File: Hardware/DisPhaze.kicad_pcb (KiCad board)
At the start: 2 copper layers, 60 x 110 mm, 76 parts, among them J1 SWD_Header, J2 PItch_In, J3 PD1_Amt_In, J4 PD2_Amt_In, J5 VCA_In, J6 DAC1_Out, J7 DAC2_Out, J8 Eurorack_16_pin_power, SW1 DAC1_RingMod_Switch, SW2 DAC2_Mix_Switch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

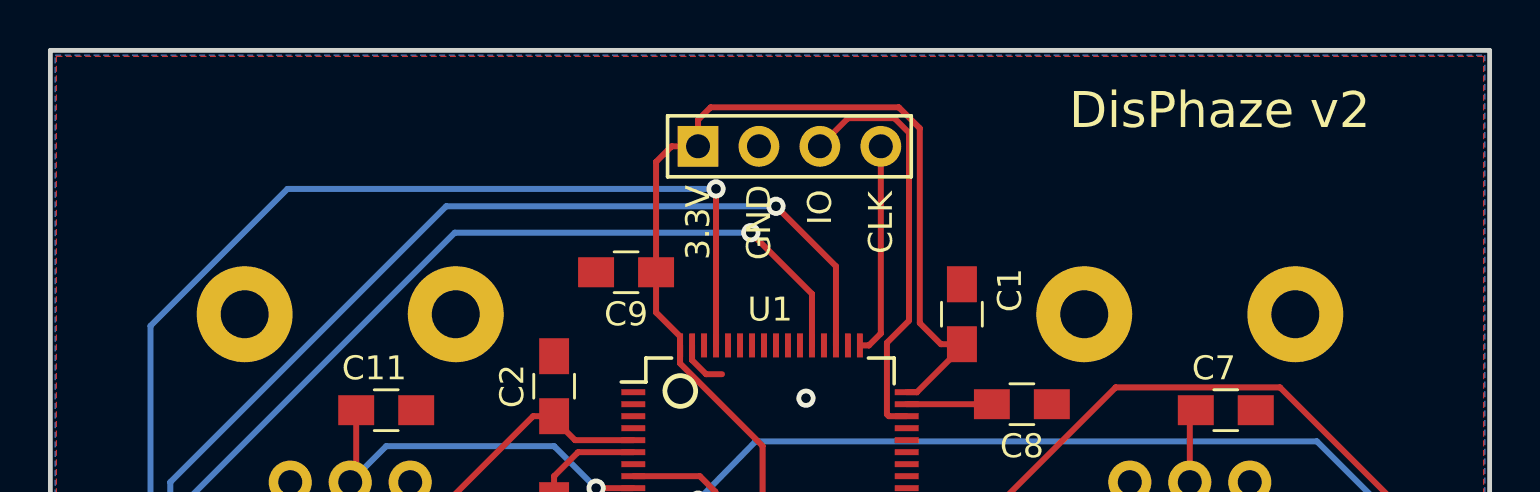
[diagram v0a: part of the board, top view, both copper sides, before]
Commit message: Added basic calibration and further tweaks to panel
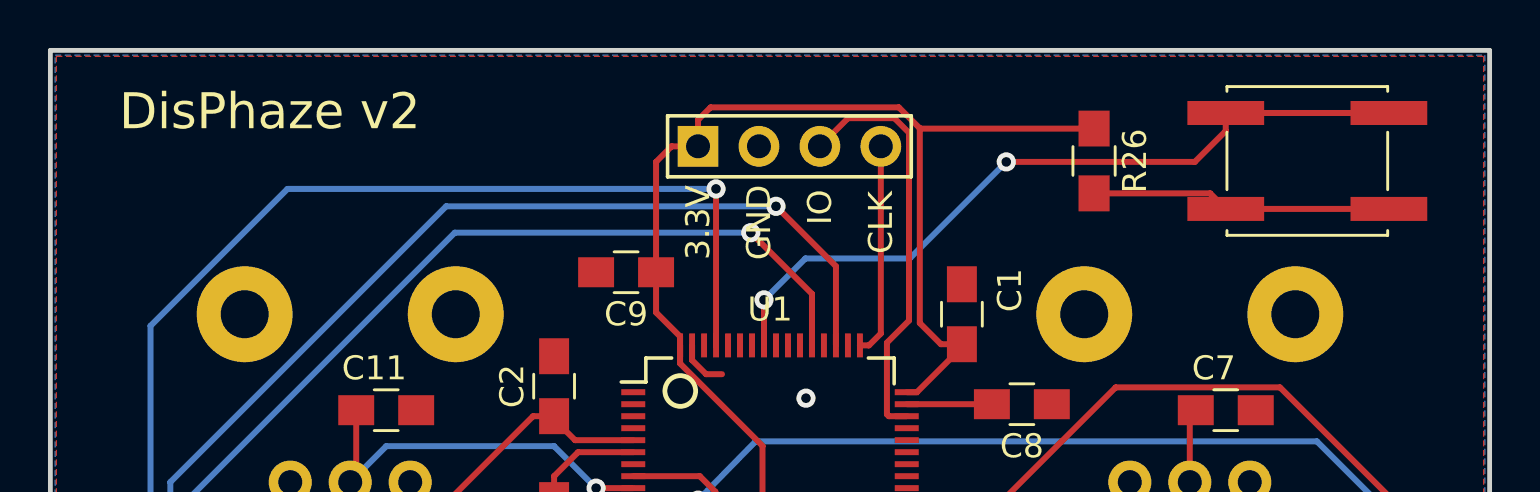
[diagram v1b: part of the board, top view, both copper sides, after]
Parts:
- added R26: 680R, Resistors_SMD:R_0805_HandSoldering, F.Cu at (143.5, 54.6)
- added SW4: SW_Push, Buttons_Switches_SMD:SW_SPST_EVQQ2, F.Cu at (152.4, 54.6)
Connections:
- U1 pad 57: Net-(U1-Pad57) -> Calibration
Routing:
- net Calibration: track 0.00 -> 31.6 mm, vias 0 -> 2
- net Net-(R26-Pad2): track 0.00 -> 12.6 mm
- net +3V3: track 187.6 -> 194.9 mm
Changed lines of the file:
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@@
     (thickness 1.6)
     (drawings 29)
-    (tracks 483)
+    (tracks 498)
     (zones 0)
-    (modules 76)
-    (nets 92)
+    (modules 78)
+    (nets 93)
   )
   (page A4)
@@
   )
   (setup
-    (last_trace_width 0.5)
+    (last_trace_width 0.25)
     (user_trace_width 0.5)
     (trace_clearance 0.2)
@@
   (net 83 "Net-(U1-Pad55)")
   (net 84 "Net-(U1-Pad56)")
-  (net 85 "Net-(U1-Pad57)")
-  (net 86 "Net-(U1-Pad58)")
-  (net 87 "Net-(U1-Pad59)")
-  (net 88 "Net-(U1-Pad60)")
-  (net 89 "Net-(U1-Pad62)")
-  (net 90 "Net-(U1-Pad33)")
-  (net 91 "Net-(U1-Pad34)")
+  (net 85 "Net-(U1-Pad58)")
+  (net 86 "Net-(U1-Pad59)")
+  (net 87 "Net-(U1-Pad60)")
+  (net 88 "Net-(U1-Pad62)")
+  (net 89 "Net-(U1-Pad33)")
+  (net 90 "Net-(U1-Pad34)")
+  (net 91 Calibration)
+  (net 92 "Net-(R26-Pad2)")
   (net_class Default "This is the default net class."
     (clearance 0.2)
@@
     (add_net CTUNE)
     (add_net CV_IN)
+    (add_net Calibration)
     (add_net DAC1_OUT)
     (add_net DAC1_RING_MOD)
@@
     (add_net "Net-(R21-Pad2)")
     (add_net "Net-(R22-Pad2)")
+    (add_net "Net-(R26-Pad2)")
     (add_net "Net-(U1-Pad1)")
     (add_net "Net-(U1-Pad11)")
@@
     (add_net "Net-(U1-Pad55)")
     (add_net "Net-(U1-Pad56)")
-    (add_net "Net-(U1-Pad57)")
     (add_net "Net-(U1-Pad58)")
     (add_net "Net-(U1-Pad59)")
@@
       (net 2 +3V3))
     (pad 33 smd rect (at 5.7 3.75) (size 1 0.25) (layers F.Cu F.Paste F.Mask)
-      (net 90 "Net-(U1-Pad33)"))
+      (net 89 "Net-(U1-Pad33)"))
     (pad 34 smd rect (at 5.7 3.25) (size 1 0.25) (layers F.Cu F.Paste F.Mask)
-      (net 91 "Net-(U1-Pad34)"))
+      (net 90 "Net-(U1-Pad34)"))
     (pad 35 smd rect (at 5.7 2.75) (size 1 0.25) (layers F.Cu F.Paste F.Mask)
       (net 70 "Net-(U1-Pad35)"))
@@
       (net 84 "Net-(U1-Pad56)"))
     (pad 57 smd rect (at -0.25 -5.7 90) (size 1 0.25) (layers F.Cu F.Paste F.Mask)
-      (net 85 "Net-(U1-Pad57)"))
+      (net 91 Calibration))
     (pad 58 smd rect (at -0.75 -5.7 90) (size 1 0.25) (layers F.Cu F.Paste F.Mask)
-      (net 86 "Net-(U1-Pad58)"))
+      (net 85 "Net-(U1-Pad58)"))
     (pad 59 smd rect (at -1.25 -5.7 90) (size 1 0.25) (layers F.Cu F.Paste F.Mask)
-      (net 87 "Net-(U1-Pad59)"))
+      (net 86 "Net-(U1-Pad59)"))
     (pad 60 smd rect (at -1.75 -5.7 90) (size 1 0.25) (layers F.Cu F.Paste F.Mask)
-      (net 88 "Net-(U1-Pad60)"))
+      (net 87 "Net-(U1-Pad60)"))
     (pad 61 smd rect (at -2.25 -5.7 90) (size 1 0.25) (layers F.Cu F.Paste F.Mask)
       (net 55 DAC2_MIX))
     (pad 62 smd rect (at -2.75 -5.7 90) (size 1 0.25) (layers F.Cu F.Paste F.Mask)
-      (net 89 "Net-(U1-Pad62)"))
+      (net 88 "Net-(U1-Pad62)"))
     (pad 63 smd rect (at -3.25 -5.7 90) (size 1 0.25) (layers F.Cu F.Paste F.Mask)
       (net 1 GND))
@@
     )
   )
+  (module Buttons_Switches_SMD:SW_SPST_EVQQ2 (layer F.Cu)
+    (at 152.4 54.61)
+    (descr "Light Touch Switch, https://industrial.panasonic.com/cdbs/www-data/pdf/ATK0000/ATK0000CE28.pdf")
+    (attr smd)
+    (fp_text reference SW4 (at 0.05 -3.95) (layer F.SilkS) hide
+      (effects (font (size 1 1) (thickness 0.15)))
+    )
+    (fp_text value SW_Push (at 0 4.25) (layer F.Fab)
+      (effects (font (size 1 1) (thickness 0.15)))
+    )
+    (fp_circle (center 0 0) (end 1.5 0) (layer F.Fab) (width 0.1))
+    (fp_circle (center 0 0) (end 1.9 0) (layer F.Fab) (width 0.1))
+    (fp_line (start -3.35 3.1) (end 3.35 3.1) (layer F.SilkS) (width 0.12))
+    (fp_line (start 3.35 -3.1) (end -3.35 -3.1) (layer F.SilkS) (width 0.12))
+    (fp_line (start 3.35 -1.2) (end 3.35 1.2) (layer F.SilkS) (width 0.12))
+    (fp_line (start -3.35 -1.2) (end -3.35 1.2) (layer F.SilkS) (width 0.12))
+    (fp_line (start -3.35 -3.1) (end -3.35 -2.9) (layer F.SilkS) (width 0.12))
+    (fp_line (start -3.35 3.1) (end -3.35 2.9) (layer F.SilkS) (width 0.12))
+    (fp_line (start 3.35 3.1) (end 3.35 2.9) (layer F.SilkS) (width 0.12))
+    (fp_line (start 3.35 -3.1) (end 3.35 -2.9) (layer F.SilkS) (width 0.12))
+    (fp_line (start -5.25 3.25) (end -5.25 -3.25) (layer F.CrtYd) (width 0.05))
+    (fp_line (start 5.25 3.25) (end -5.25 3.25) (layer F.CrtYd) (width 0.05))
+    (fp_line (start 5.25 -3.25) (end 5.25 3.25) (layer F.CrtYd) (width 0.05))
+    (fp_line (start -5.25 -3.25) (end 5.25 -3.25) (layer F.CrtYd) (width 0.05))
+    (fp_text user %R (at 0.05 -3.95) (layer F.Fab)
+      (effects (font (size 1 1) (thickness 0.15)))
+    )
+    (fp_line (start -3.25 3) (end -3.25 -3) (layer F.Fab) (width 0.1))
+    (fp_line (start 3.25 3) (end -3.25 3) (layer F.Fab) (width 0.1))
+    (fp_line (start 3.25 -3) (end 3.25 3) (layer F.Fab) (width 0.1))
+    (fp_line (start -3.25 -3) (end 3.25 -3) (layer F.Fab) (width 0.1))
+    (pad 2 smd rect (at 3.4 2) (size 3.2 1) (layers F.Cu F.Paste F.Mask)
+      (net 92 "Net-(R26-Pad2)"))
+    (pad 2 smd rect (at -3.4 2) (size 3.2 1) (layers F.Cu F.Paste F.Mask)
+      (net 92 "Net-(R26-Pad2)"))
+    (pad 1 smd rect (at -3.4 -2) (size 3.2 1) (layers F.Cu F.Paste F.Mask)
+      (net 91 Calibration))
+    (pad 1 smd rect (at 3.4 -2) (size 3.2 1) (layers F.Cu F.Paste F.Mask)
+      (net 91 Calibration))
+    (model Buttons_Switches_SMD.3dshapes\SW_SPST_EVQQ2.wrl
+      (at (xyz 0 0 0))
+      (scale (xyz 1 1 1))
+      (rotate (xyz 0 0 0))
+    )
+  )
+  (module Resistors_SMD:R_0805_HandSoldering (layer F.Cu)
+    (at 143.51 54.61 270)
+    (descr "Resistor SMD 0805, hand soldering")
+    (tags "resistor 0805")
+    (attr smd)
+    (fp_text reference R26 (at 0 -1.7 270) (layer F.SilkS)
+      (effects (font (size 1 1) (thickness 0.15)))
+    )
+    (fp_text value 680R (at 0 1.75 270) (layer F.Fab)
+      (effects (font (size 1 1) (thickness 0.15)))
+    )
+    (fp_line (start 2.35 0.9) (end -2.35 0.9) (layer F.CrtYd) (width 0.05))
+    (fp_line (start 2.35 0.9) (end 2.35 -0.9) (layer F.CrtYd) (width 0.05))
+    (fp_line (start -2.35 -0.9) (end -2.35 0.9) (layer F.CrtYd) (width 0.05))
+    (fp_line (start -2.35 -0.9) (end 2.35 -0.9) (layer F.CrtYd) (width 0.05))
+    (fp_line (start -0.6 -0.88) (end 0.6 -0.88) (layer F.SilkS) (width 0.12))
+    (fp_line (start 0.6 0.88) (end -0.6 0.88) (layer F.SilkS) (width 0.12))
+    (fp_line (start -1 -0.62) (end 1 -0.62) (layer F.Fab) (width 0.1))
+    (fp_line (start 1 -0.62) (end 1 0.62) (layer F.Fab) (width 0.1))
+    (fp_line (start 1 0.62) (end -1 0.62) (layer F.Fab) (width 0.1))
+    (fp_line (start -1 0.62) (end -1 -0.62) (layer F.Fab) (width 0.1))
+    (fp_text user %R (at 0 0 270) (layer F.Fab)
+      (effects (font (size 0.5 0.5) (thickness 0.075)))
+    )
+    (pad 2 smd rect (at 1.35 0 270) (size 1.5 1.3) (layers F.Cu F.Paste F.Mask)
+      (net 92 "Net-(R26-Pad2)"))
+    (pad 1 smd rect (at -1.35 0 270) (size 1.5 1.3) (layers F.Cu F.Paste F.Mask)
+      (net 2 +3V3))
+    (model ${KISYS3DMOD}/Resistors_SMD.3dshapes/R_0805.wrl
+      (at (xyz 0 0 0))
+      (scale (xyz 1 1 1))
+      (rotate (xyz 0 0 0))
+    )
+  )
   (gr_circle (center 113.25 120.5) (end 114.25 121.5) (layer F.SilkS) (width 0.2))
   (gr_circle (center 125.5 118.5) (end 126.5 119.5) (layer F.SilkS) (width 0.2))
@@
   )
   (gr_circle (center 126.259688 64.2) (end 126.759688 64.6) (layer F.SilkS) (width 0.2))
-  (gr_text "DisPhaze v2" (at 148.75 52.5) (layer F.SilkS)
+  (gr_text "DisPhaze v2" (at 109.15 52.55) (layer F.SilkS)
     (effects (font (size 1.5 1.5) (thickness 0.3)))
   )
@@
   (segment (start 151.35 124.6) (end 150 123.25) (width 0.5) (layer F.Cu) (net 2))
   (segment (start 151.35 128.5) (end 151.35 124.6) (width 0.5) (layer F.Cu) (net 2))
+  (segment (start 136.255412 53.26) (end 136.24501 53.249598) (width 0.25) (layer F.Cu) (net 2))
+  (segment (start 143.51 53.26) (end 136.255412 53.26) (width 0.25) (layer F.Cu) (net 2))
   (segment (start 121 65.375) (end 121 65.25) (width 0.25) (layer F.Cu) (net 3) (status 30))
   (segment (start 121.875 66.25) (end 121 65.375) (width 0.25) (layer F.Cu) (net 3) (status 20))
@@
   (segment (start 116.858998 57.6) (end 105.774999 68.683999) (width 0.25) (layer B.Cu) (net 57))
   (segment (start 129.2 57.6) (end 116.858998 57.6) (width 0.25) (layer B.Cu) (net 57))
+  (via (at 129.75 60.4) (size 0.8) (drill 0.4) (layers F.Cu B.Cu) (net 91))
+  (segment (start 129.75 62.3) (end 129.75 60.4) (width 0.25) (layer F.Cu) (net 91))
+  (via (at 139.85 54.65) (size 0.8) (drill 0.4) (layers F.Cu B.Cu) (net 91))
+  (segment (start 135.825001 58.674999) (end 139.85 54.65) (width 0.25) (layer B.Cu) (net 91))
+  (segment (start 129.75 60.4) (end 131.475001 58.674999) (width 0.25) (layer B.Cu) (net 91))
+  (segment (start 131.475001 58.674999) (end 135.825001 58.674999) (width 0.25) (layer B.Cu) (net 91))
+  (segment (start 149 53.36) (end 149 52.61) (width 0.25) (layer F.Cu) (net 91))
+  (segment (start 147.71 54.65) (end 149 53.36) (width 0.25) (layer F.Cu) (net 91))
+  (segment (start 139.85 54.65) (end 147.71 54.65) (width 0.25) (layer F.Cu) (net 91))
+  (segment (start 149 52.61) (end 155.8 52.61) (width 0.25) (layer F.Cu) (net 91))
+  (segment (start 155.8 56.61) (end 149 56.61) (width 0.25) (layer F.Cu) (net 92))
+  (segment (start 148.35 55.96) (end 149 56.61) (width 0.25) (layer F.Cu) (net 92))
+  (segment (start 143.51 55.96) (end 148.35 55.96) (width 0.25) (layer F.Cu) (net 92))
   (zone (net 1) (net_name GND) (layer B.Cu) (hatch edge 0.508)
     (connect_pads (clearance 0.508))

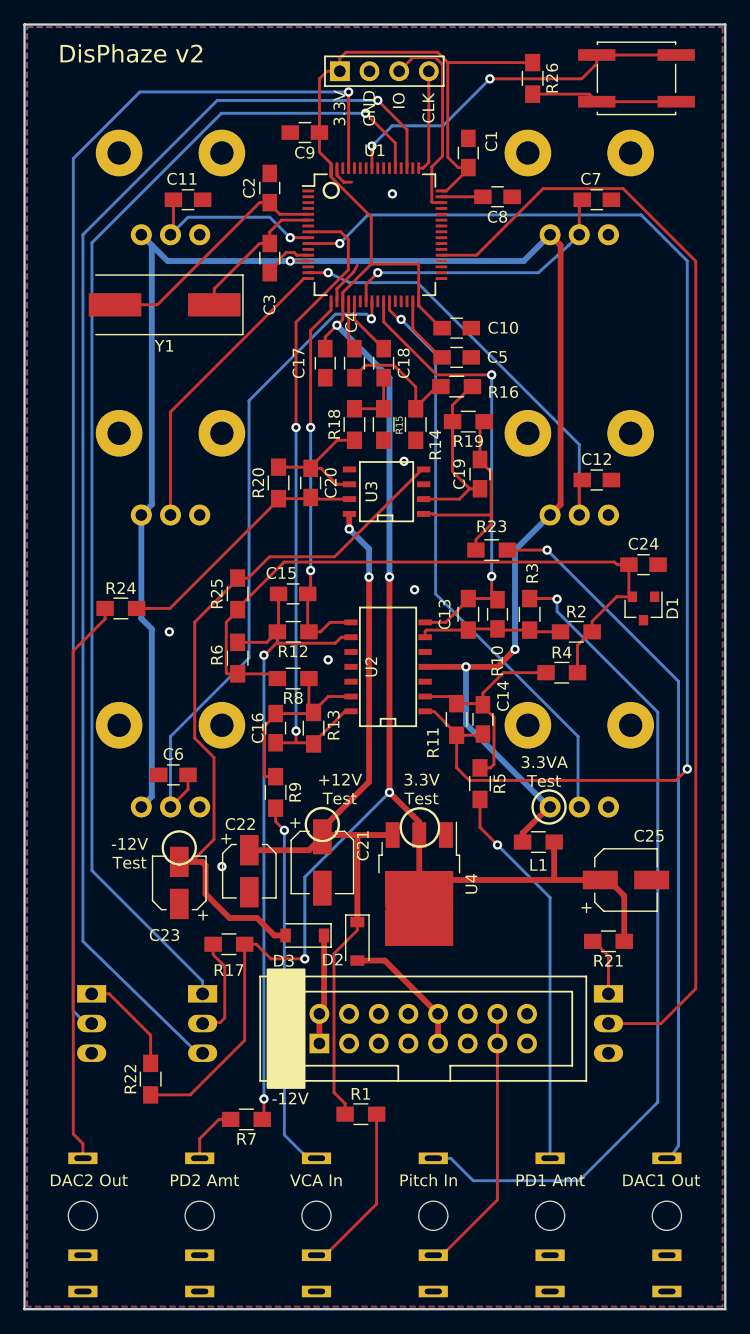
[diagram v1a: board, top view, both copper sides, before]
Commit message: Calibration settings can be saved to Flash memory and finalised PCB and panel for manufacture
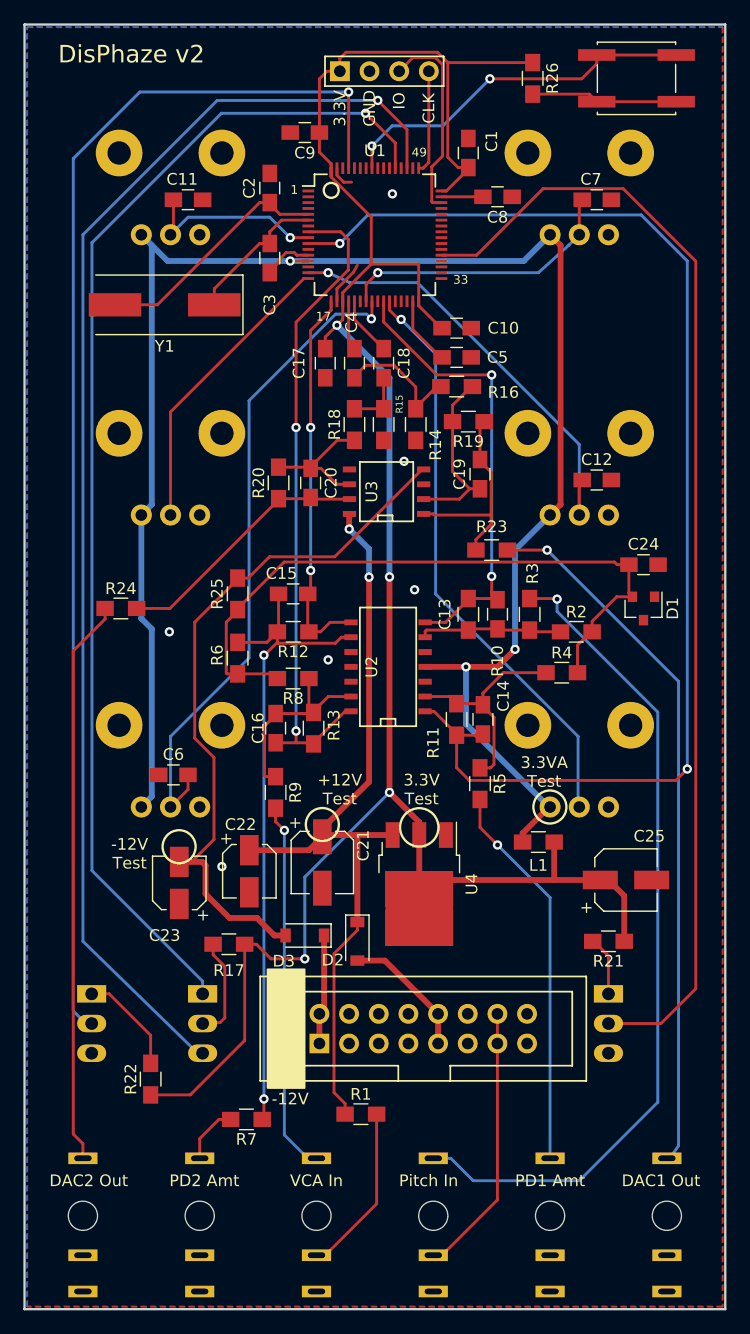
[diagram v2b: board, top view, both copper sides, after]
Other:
- board text added: "1"
- board text added: "17"
- board text added: "33"
- board text added: "49"
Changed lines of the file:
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@@
   (general
     (thickness 1.6)
-    (drawings 29)
+    (drawings 33)
     (tracks 498)
     (zones 0)
@@
       (outputformat 1)
       (mirror false)
-      (drillshape 1)
+      (drillshape 0)
       (scaleselection 1)
-      (outputdirectory ""))
+      (outputdirectory "Gerbers/PCB/"))
   )
   (net 0 "")
@@
     (tags "resistor 0805")
     (attr smd)
-    (fp_text reference R15 (at 0.05 -1.35 270) (layer F.SilkS)
+    (fp_text reference R15 (at -1.75 -1.35 270) (layer F.SilkS)
       (effects (font (size 0.6 0.6) (thickness 0.1)))
     )
@@
     )
   )
-  (gr_circle (center 113.25 120.5) (end 114.25 121.5) (layer F.SilkS) (width 0.2))
+  (gr_text 1 (at 123.1 64.15) (layer F.SilkS)
+    (effects (font (size 0.75 0.75) (thickness 0.1)))
+  )
+  (gr_text 49 (at 133.8 60.95) (layer F.SilkS)
+    (effects (font (size 0.75 0.75) (thickness 0.1)))
+  )
+  (gr_text 33 (at 137.35 71.85) (layer F.SilkS)
+    (effects (font (size 0.75 0.75) (thickness 0.1)))
+  )
+  (gr_text 17 (at 125.6 75) (layer F.SilkS)
+    (effects (font (size 0.75 0.75) (thickness 0.1)))
+  )
+  (gr_circle (center 113.235787 120.4) (end 114.235787 121.4) (layer F.SilkS) (width 0.2))
   (gr_circle (center 125.5 118.5) (end 126.5 119.5) (layer F.SilkS) (width 0.2))
-  (gr_circle (center 133.857678 118.75) (end 134.857678 120.052775) (layer F.SilkS) (width 0.2))
+  (gr_circle (center 133.8 118.742322) (end 134.8 120.045097) (layer F.SilkS) (width 0.2))
   (gr_text "3.3V\nTest" (at 134 115.5) (layer F.SilkS)
     (effects (font (size 1 1) (thickness 0.2)))
   )
-  (gr_circle (center 144.914213 117) (end 145.914213 118) (layer F.SilkS) (width 0.2))
+  (gr_circle (center 144.985787 117) (end 145.985787 118) (layer F.SilkS) (width 0.2))
   (gr_text "3.3VA\nTest" (at 144.5 114) (layer F.SilkS)
     (effects (font (size 1 1) (thickness 0.2)))
